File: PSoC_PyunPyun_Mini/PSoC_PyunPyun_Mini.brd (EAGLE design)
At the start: 56.8 x 49.5 mm, 24 parts, among them IC1 LM358N

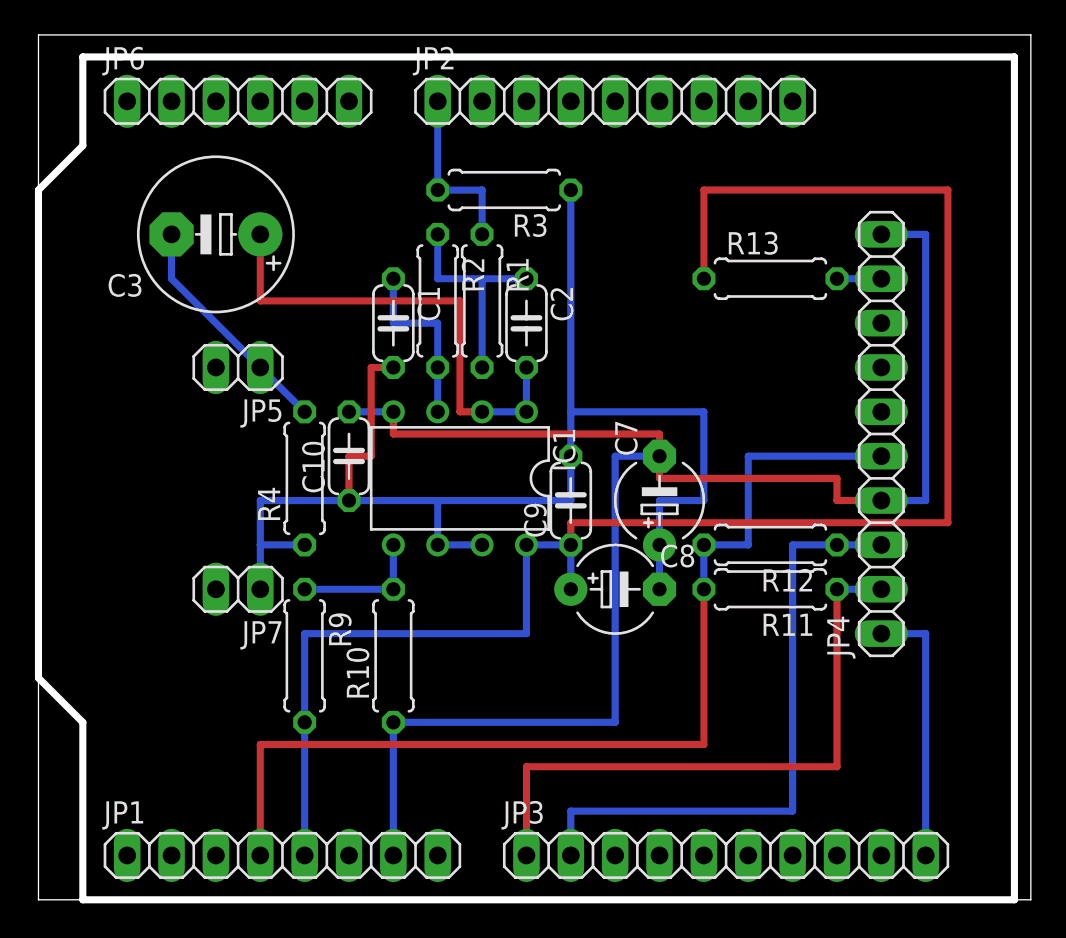
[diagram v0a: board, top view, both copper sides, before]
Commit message: PSoC_PyunPyun_Mini ボード図変更 LCDの位置を上にずらした
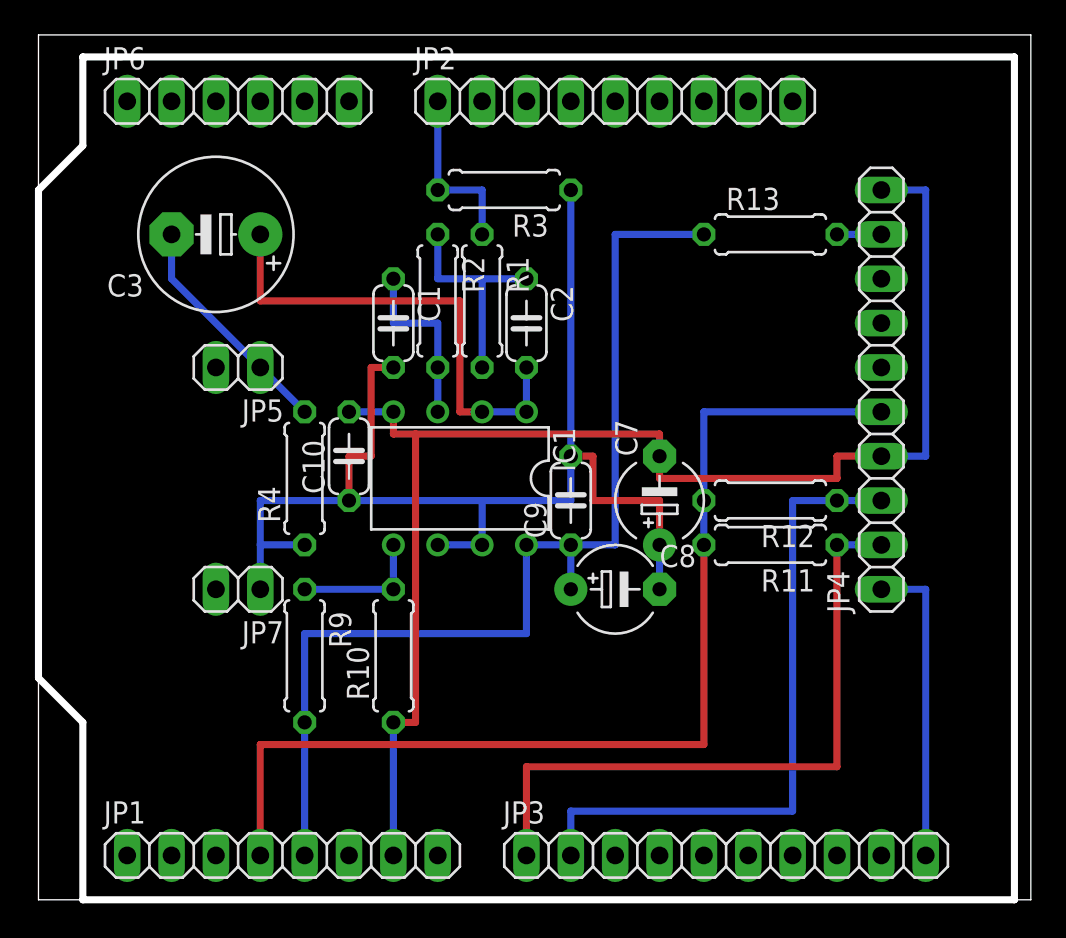
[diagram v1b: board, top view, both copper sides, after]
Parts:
- moved JP4 2.54 mm to (48.3, 29.2)
- moved R11 2.54 mm to (41.9, 20.3)
- moved R12 2.54 mm to (41.9, 22.9)
- moved R13 2.54 mm to (41.9, 38.1)
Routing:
- net +5V: track 96.5 -> 61.0 mm
- net GND: track 94.0 -> 81.3 mm
- net AGND: track 78.7 -> 71.1 mm
- net SDA: track 35.6 -> 38.1 mm
- net +3.3V: track 58.4 -> 61.0 mm
- net RST: track 15.2 -> 17.8 mm
- net SCL: track 35.6 -> 38.1 mm
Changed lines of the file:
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@@
 <element name="JP2" library="pinhead" package="1X09" value="" x="33.02" y="45.72"/>
 <element name="JP3" library="pinhead" package="1X10" value="" x="39.37" y="2.54"/>
-<element name="JP4" library="pinhead" package="1X10" value="I2C-LCD" x="48.26" y="26.67" rot="R90"/>
+<element name="JP4" library="pinhead" package="1X10" value="I2C-LCD" x="48.26" y="29.21" rot="R90"/>
 <element name="JP5" library="pinhead" package="1X02" value="RCA_HOT" x="11.43" y="30.48" rot="R180"/>
 <element name="R1" library="rcl" package="0207/7" value="10k" x="25.4" y="34.29" rot="R270"/>
 <element name="R10" library="rcl" package="0207/7" value="10k" x="20.32" y="13.97" rot="R90"/>
-<element name="R11" library="rcl" package="0207/7" value="3.3k" x="41.91" y="17.78" rot="R180"/>
-<element name="R12" library="rcl" package="0207/7" value="3.3k" x="41.91" y="20.32" rot="R180"/>
-<element name="R13" library="rcl" package="0207/7" value="330" x="41.91" y="35.56"/>
+<element name="R11" library="rcl" package="0207/7" value="3.3k" x="41.91" y="20.32" rot="R180"/>
+<element name="R12" library="rcl" package="0207/7" value="3.3k" x="41.91" y="22.86" rot="R180"/>
+<element name="R13" library="rcl" package="0207/7" value="330" x="41.91" y="38.1"/>
 <element name="R2" library="rcl" package="0207/7" value="10k" x="22.86" y="34.29" rot="R270"/>
 <element name="R3" library="rcl" package="0207/7" value="2.2k" x="26.67" y="40.64" rot="R180"/>
@@
 <contactref element="C10" pad="2"/>
 <wire x1="17.78" y1="27.94" x2="20.32" y2="27.94" width="0.4064" layer="16"/>
-<wire x1="20.32" y1="10.16" x2="33.02" y2="10.16" width="0.4064" layer="16"/>
-<wire x1="33.02" y1="10.16" x2="33.02" y2="25.4" width="0.4064" layer="16"/>
-<wire x1="33.02" y1="25.4" x2="35.56" y2="25.4" width="0.4064" layer="16"/>
-<wire x1="48.26" y1="22.86" x2="50.8" y2="22.86" width="0.4064" layer="16"/>
-<wire x1="50.8" y1="22.86" x2="50.8" y2="38.1" width="0.4064" layer="16"/>
-<wire x1="50.8" y1="38.1" x2="48.26" y2="38.1" width="0.4064" layer="16"/>
+<wire x1="48.26" y1="25.4" x2="50.8" y2="25.4" width="0.4064" layer="16"/>
+<wire x1="50.8" y1="25.4" x2="50.8" y2="40.64" width="0.4064" layer="16"/>
+<wire x1="50.8" y1="40.64" x2="48.26" y2="40.64" width="0.4064" layer="16"/>
 <wire x1="20.32" y1="27.94" x2="20.32" y2="26.67" width="0.4064" layer="1"/>
-<wire x1="20.32" y1="26.67" x2="35.56" y2="26.67" width="0.4064" layer="1"/>
+<wire x1="20.32" y1="26.67" x2="21.59" y2="26.67" width="0.4064" layer="1"/>
+<wire x1="21.59" y1="26.67" x2="35.56" y2="26.67" width="0.4064" layer="1"/>
 <wire x1="35.56" y1="26.67" x2="35.56" y2="25.4" width="0.4064" layer="1"/>
 <wire x1="35.56" y1="25.4" x2="35.56" y2="24.13" width="0.4064" layer="1"/>
 <wire x1="35.56" y1="24.13" x2="45.72" y2="24.13" width="0.4064" layer="1"/>
-<wire x1="45.72" y1="24.13" x2="45.72" y2="22.86" width="0.4064" layer="1"/>
-<wire x1="45.72" y1="22.86" x2="48.26" y2="22.86" width="0.4064" layer="1"/>
+<wire x1="45.72" y1="24.13" x2="45.72" y2="25.4" width="0.4064" layer="1"/>
+<wire x1="45.72" y1="25.4" x2="48.26" y2="25.4" width="0.4064" layer="1"/>
+<wire x1="20.32" y1="10.16" x2="21.59" y2="10.16" width="0.4064" layer="1"/>
+<wire x1="21.59" y1="10.16" x2="21.59" y2="26.67" width="0.4064" layer="1"/>
 </signal>
 <signal name="N$8">
@@
 <wire x1="27.94" y1="15.24" x2="27.94" y2="20.32" width="0.4064" layer="16"/>
 <wire x1="30.48" y1="17.78" x2="30.48" y2="20.32" width="0.4064" layer="16"/>
-<wire x1="38.1" y1="35.56" x2="38.1" y2="40.64" width="0.4064" layer="1"/>
-<wire x1="38.1" y1="40.64" x2="52.07" y2="40.64" width="0.4064" layer="1"/>
-<wire x1="52.07" y1="40.64" x2="52.07" y2="21.59" width="0.4064" layer="1"/>
-<wire x1="52.07" y1="21.59" x2="30.48" y2="21.59" width="0.4064" layer="1"/>
-<wire x1="30.48" y1="21.59" x2="30.48" y2="20.32" width="0.4064" layer="1"/>
+<wire x1="30.48" y1="20.32" x2="33.02" y2="20.32" width="0.4064" layer="16"/>
+<wire x1="33.02" y1="20.32" x2="33.02" y2="38.1" width="0.4064" layer="16"/>
+<wire x1="33.02" y1="38.1" x2="38.1" y2="38.1" width="0.4064" layer="16"/>
 </signal>
 <signal name="AGND">
@@
 <contactref element="C10" pad="1"/>
 <contactref element="C9" pad="2"/>
-<wire x1="22.86" y1="20.32" x2="22.86" y2="22.86" width="0.4064" layer="16"/>
-<wire x1="17.78" y1="22.86" x2="22.86" y2="22.86" width="0.4064" layer="16"/>
-<wire x1="22.86" y1="22.86" x2="30.48" y2="22.86" width="0.4064" layer="16"/>
-<wire x1="30.48" y1="22.86" x2="30.48" y2="25.4" width="0.4064" layer="16"/>
 <wire x1="17.78" y1="22.86" x2="12.7" y2="22.86" width="0.4064" layer="16"/>
 <wire x1="12.7" y1="22.86" x2="12.7" y2="20.32" width="0.4064" layer="16"/>
 <wire x1="12.7" y1="20.32" x2="12.7" y2="17.78" width="0.4064" layer="16"/>
 <wire x1="15.24" y1="20.32" x2="12.7" y2="20.32" width="0.4064" layer="16"/>
-<wire x1="30.48" y1="40.64" x2="30.48" y2="27.94" width="0.4064" layer="16"/>
-<wire x1="30.48" y1="27.94" x2="30.48" y2="25.4" width="0.4064" layer="16"/>
 <wire x1="35.56" y1="20.32" x2="35.56" y2="17.78" width="0.4064" layer="16"/>
-<wire x1="35.56" y1="20.32" x2="35.56" y2="22.86" width="0.4064" layer="16"/>
-<wire x1="35.56" y1="22.86" x2="38.1" y2="22.86" width="0.4064" layer="16"/>
-<wire x1="38.1" y1="22.86" x2="38.1" y2="27.94" width="0.4064" layer="16"/>
-<wire x1="38.1" y1="27.94" x2="30.48" y2="27.94" width="0.4064" layer="16"/>
 <wire x1="20.32" y1="30.48" x2="19.05" y2="30.48" width="0.4064" layer="1"/>
 <wire x1="19.05" y1="30.48" x2="19.05" y2="25.4" width="0.4064" layer="1"/>
 <wire x1="19.05" y1="25.4" x2="17.78" y2="25.4" width="0.4064" layer="1"/>
 <wire x1="17.78" y1="25.4" x2="17.78" y2="22.86" width="0.4064" layer="1"/>
+<wire x1="17.78" y1="22.86" x2="25.4" y2="22.86" width="0.4064" layer="16"/>
+<wire x1="25.4" y1="22.86" x2="30.48" y2="22.86" width="0.4064" layer="16"/>
+<wire x1="30.48" y1="22.86" x2="30.48" y2="25.4" width="0.4064" layer="16"/>
+<wire x1="25.4" y1="20.32" x2="25.4" y2="22.86" width="0.4064" layer="16"/>
+<wire x1="30.48" y1="40.64" x2="30.48" y2="25.4" width="0.4064" layer="16"/>
+<wire x1="35.56" y1="20.32" x2="35.56" y2="22.86" width="0.4064" layer="1"/>
+<wire x1="35.56" y1="22.86" x2="31.75" y2="22.86" width="0.4064" layer="1"/>
+<wire x1="31.75" y1="22.86" x2="31.75" y2="25.4" width="0.4064" layer="1"/>
+<wire x1="31.75" y1="25.4" x2="30.48" y2="25.4" width="0.4064" layer="1"/>
 </signal>
 <signal name="+3.3V">
@@
 <contactref element="R11" pad="2"/>
 <contactref element="R12" pad="2"/>
-<wire x1="38.1" y1="17.78" x2="38.1" y2="20.32" width="0.4064" layer="16"/>
-<wire x1="38.1" y1="20.32" x2="40.64" y2="20.32" width="0.4064" layer="16"/>
-<wire x1="40.64" y1="20.32" x2="40.64" y2="25.4" width="0.4064" layer="16"/>
-<wire x1="40.64" y1="25.4" x2="48.26" y2="25.4" width="0.4064" layer="16"/>
 <wire x1="12.7" y1="2.54" x2="12.7" y2="8.89" width="0.4064" layer="1"/>
 <wire x1="12.7" y1="8.89" x2="38.1" y2="8.89" width="0.4064" layer="1"/>
-<wire x1="38.1" y1="8.89" x2="38.1" y2="17.78" width="0.4064" layer="1"/>
+<wire x1="38.1" y1="8.89" x2="38.1" y2="20.32" width="0.4064" layer="1"/>
+<wire x1="38.1" y1="20.32" x2="38.1" y2="22.86" width="0.4064" layer="16"/>
+<wire x1="38.1" y1="22.86" x2="38.1" y2="27.94" width="0.4064" layer="16"/>
+<wire x1="38.1" y1="27.94" x2="48.26" y2="27.94" width="0.4064" layer="16"/>
 </signal>
 <signal name="RST">
 <contactref element="JP3" pad="10"/>
 <contactref element="JP4" pad="1"/>
-<wire x1="50.8" y1="2.54" x2="50.8" y2="15.24" width="0.4064" layer="16"/>
-<wire x1="50.8" y1="15.24" x2="48.26" y2="15.24" width="0.4064" layer="16"/>
+<wire x1="50.8" y1="2.54" x2="50.8" y2="17.78" width="0.4064" layer="16"/>
+<wire x1="50.8" y1="17.78" x2="48.26" y2="17.78" width="0.4064" layer="16"/>
 </signal>
 <signal name="SCL">
@@
 <contactref element="JP4" pad="2"/>
 <contactref element="R11" pad="1"/>
-<wire x1="45.72" y1="17.78" x2="48.26" y2="17.78" width="0.4064" layer="16"/>
+<wire x1="45.72" y1="20.32" x2="48.26" y2="20.32" width="0.4064" layer="16"/>
 <wire x1="27.94" y1="2.54" x2="27.94" y2="7.62" width="0.4064" layer="1"/>
 <wire x1="27.94" y1="7.62" x2="45.72" y2="7.62" width="0.4064" layer="1"/>
-<wire x1="45.72" y1="7.62" x2="45.72" y2="17.78" width="0.4064" layer="1"/>
+<wire x1="45.72" y1="7.62" x2="45.72" y2="20.32" width="0.4064" layer="1"/>
 </signal>
 <signal name="SDA">
@@
 <contactref element="JP4" pad="3"/>
 <contactref element="R12" pad="1"/>
-<wire x1="45.72" y1="20.32" x2="48.26" y2="20.32" width="0.4064" layer="16"/>
-<wire x1="45.72" y1="20.32" x2="43.18" y2="20.32" width="0.4064" layer="16"/>
-<wire x1="43.18" y1="20.32" x2="43.18" y2="5.08" width="0.4064" layer="16"/>
+<wire x1="45.72" y1="22.86" x2="48.26" y2="22.86" width="0.4064" layer="16"/>
+<wire x1="45.72" y1="22.86" x2="43.18" y2="22.86" width="0.4064" layer="16"/>
+<wire x1="43.18" y1="22.86" x2="43.18" y2="5.08" width="0.4064" layer="16"/>
 <wire x1="43.18" y1="5.08" x2="30.48" y2="5.08" width="0.4064" layer="16"/>
 <wire x1="30.48" y1="5.08" x2="30.48" y2="2.54" width="0.4064" layer="16"/>
@@
 <contactref element="R13" pad="2"/>
 <contactref element="JP4" pad="9"/>
-<wire x1="45.72" y1="35.56" x2="48.26" y2="35.56" width="0.4064" layer="16"/>
+<wire x1="45.72" y1="38.1" x2="48.26" y2="38.1" width="0.4064" layer="16"/>
 </signal>
 </signals>
